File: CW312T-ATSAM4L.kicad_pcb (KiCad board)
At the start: 2 copper layers, 58.7 x 53.7 mm, 30 parts, among them J1 614105150721, P1 PCIEx4 EDGE CONNECTOR, U1 ATSAM4LC2AA-AU

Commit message: updated schematic, pcb, and production files - ready for review
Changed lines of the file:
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@@
 		(tags "resistor")
 		(property "Reference" "R9"
-			(at -0.075 -1.55 360)
+			(at -0.075 -1.55 0)
 			(layer "F.SilkS")
 			(effects
@@
 		)
 		(property "Value" "RES_10k_0603"
-			(at 0 1.43 360)
+			(at 0 1.43 0)
 			(layer "F.Fab")
 			(effects
@@
 		)
 		(fp_text user "${REFERENCE}"
-			(at 0 0 360)
+			(at 0 0 0)
 			(layer "F.Fab")
 			(effects
@@
 		(tags "resistor")
 		(property "Reference" "R2"
-			(at 2.525 0 360)
+			(at 2.525 0 0)
 			(layer "F.SilkS")
 			(effects
@@
 		)
 		(property "Value" "RES_47k_0603"
-			(at 0 1.43 360)
+			(at 0 1.43 0)
 			(layer "F.Fab")
 			(effects
@@
 		)
 		(fp_text user "${REFERENCE}"
-			(at 0 0 360)
+			(at 0 0 0)
 			(layer "F.Fab")
 			(effects
@@
 		(sheetname "Root")
 		(sheetfile "CW312T-ATSAM4L.kicad_sch")
-		(attr smd)
+		(attr smd dnp)
 		(fp_line
 			(start -0.14058 -0.51)
@@
 		(tags "capacitor")
 		(property "Reference" "C2"
-			(at 2.525 0.06 360)
+			(at 2.525 0.06 0)
 			(layer "F.SilkS")
 			(effects
@@
 		)
 		(property "Value" "CAP_2u2_6.3V_0603"
-			(at 0 1.43 360)
+			(at 0 1.43 0)
 			(layer "F.Fab")
 			(effects
@@
 		)
 		(fp_text user "${REFERENCE}"
-			(at 0 0 360)
+			(at 0 0 0)
 			(layer "F.Fab")
 			(effects
@@
 		(sheetname "Root")
 		(sheetfile "CW312T-ATSAM4L.kicad_sch")
-		(attr through_hole)
+		(attr through_hole dnp)
 		(fp_line
 			(start -2.85 -1.38)
@@
 		(tags "capacitor")
 		(property "Reference" "C1"
-			(at -2.525 0 360)
+			(at -2.525 0 0)
 			(layer "F.SilkS")
 			(effects
@@
 		)
 		(property "Value" "CAP_100n_10V_0603"
-			(at 0 1.43 360)
+			(at 0 1.43 0)
 			(layer "F.Fab")
 			(effects
@@
 		)
 		(fp_text user "${REFERENCE}"
-			(at 0 0 360)
+			(at 0 0 0)
 			(layer "F.Fab")
 			(effects
@@
 		(tags "capacitor")
 		(property "Reference" "C12"
-			(at 0 1.95 360)
+			(at 0 1.95 0)
 			(layer "F.SilkS")
 			(effects
@@
 		)
 		(property "Value" "CAP_2u2_6.3V_0603"
-			(at 0 1.43 360)
+			(at 0 1.43 0)
 			(layer "F.Fab")
 			(effects
@@
 		)
 		(fp_text user "${REFERENCE}"
-			(at 0 0 360)
+			(at 0 0 0)
 			(layer "F.Fab")
 			(effects
@@
 		(tags "resistor")
 		(property "Reference" "R7"
-			(at -2.4 -0.1 360)
+			(at -2.4 -0.1 0)
 			(layer "F.SilkS")
 			(effects
@@
 		)
 		(property "Value" "RES_1k5_0603"
-			(at 0 1.43 360)
+			(at 0 1.43 0)
 			(layer "F.Fab")
 			(effects
@@
 		)
 		(fp_text user "${REFERENCE}"
-			(at 0 0 360)
+			(at 0 0 0)
 			(layer "F.Fab")
 			(effects
@@
 		(tags "LQFP QFP")
 		(property "Reference" "U1"
-			(at 4.300001 4.5375 360)
+			(at 4.300001 4.5375 0)
 			(layer "F.SilkS")
 			(effects
@@
 		)
 		(property "Value" "ATSAM4LC2AA-AU"
-			(at 0 5.85 360)
+			(at 0 5.85 0)
 			(layer "F.Fab")
 			(effects
@@
 		)
 		(fp_text user "${REFERENCE}"
-			(at 0 0 360)
+			(at 0 0 0)
 			(layer "F.Fab")
 			(effects
@@
 		(tags "capacitor")
 		(property "Reference" "C10"
-			(at 2.975 -0.05 360)
+			(at 2.975 -0.05 0)
 			(layer "F.SilkS")
 			(effects
@@
 		)
 		(property "Value" "CAP_100n_10V_0603"
-			(at 0 1.43 360)
+			(at 0 1.43 0)
 			(layer "F.Fab")
 			(effects
@@
 		)
 		(fp_text user "${REFERENCE}"
-			(at 0 0 360)
+			(at 0 0 0)
 			(layer "F.Fab")
 			(effects
@@
 		(tags "capacitor")
 		(property "Reference" "C3"
-			(at -2.45 0 360)
+			(at -2.45 0 0)
 			(layer "F.SilkS")
 			(effects
@@
 		)
 		(property "Value" "CAP_47p_50V_0603"
-			(at 0 1.43 360)
+			(at 0 1.43 0)
 			(layer "F.Fab")
 			(effects
@@
 		(sheetname "Root")
 		(sheetfile "CW312T-ATSAM4L.kicad_sch")
-		(attr smd)
+		(attr smd dnp)
 		(fp_line
 			(start -0.140581 0.51)
@@
 		)
 		(fp_text user "${REFERENCE}"
-			(at 0 0 360)
+			(at 0 0 0)
 			(layer "F.Fab")
 			(effects
@@
 	)
 	(gr_text "SAM4L Target Board \nFor ChipWhisperer \nCW312T Board"
-		(at 162.2 78.8 0)
+		(at 162.15 79.1 0)
 		(layer "F.SilkS")
 		(effects
@@
 		(polygon
 			(pts
-				(xy 110.65 55.3) (xy 173.7 55.3) (xy 173.7 114.15) (xy 173.7 114.15) (xy 110.65 114.15)
+				(xy 110.65 55.3) (xy 173.7 55.3) (xy 173.7 114.15) (xy 110.65 114.15)
 			)
 		)

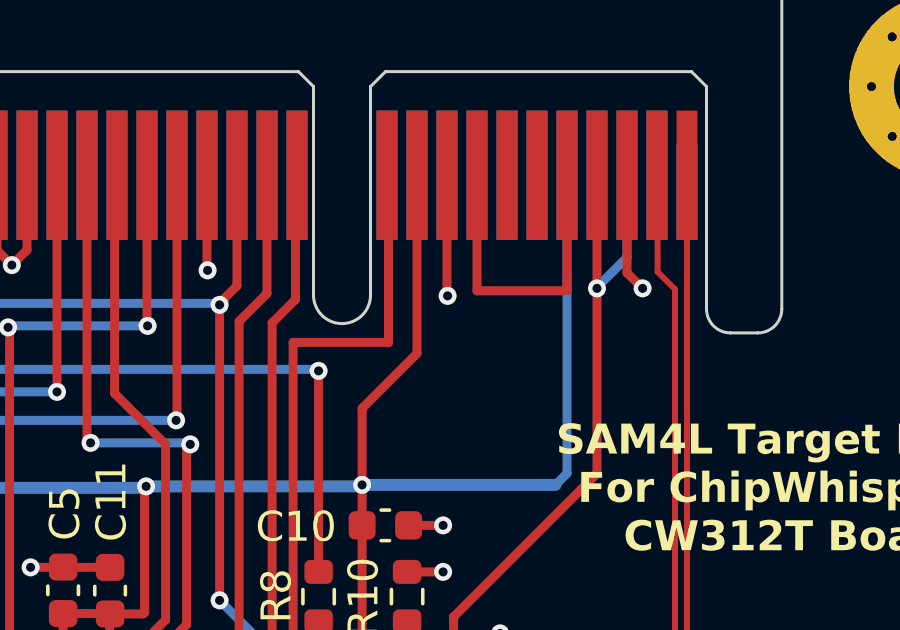
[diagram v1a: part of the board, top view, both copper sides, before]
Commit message: updated silkscreen, schematic notes, and production files
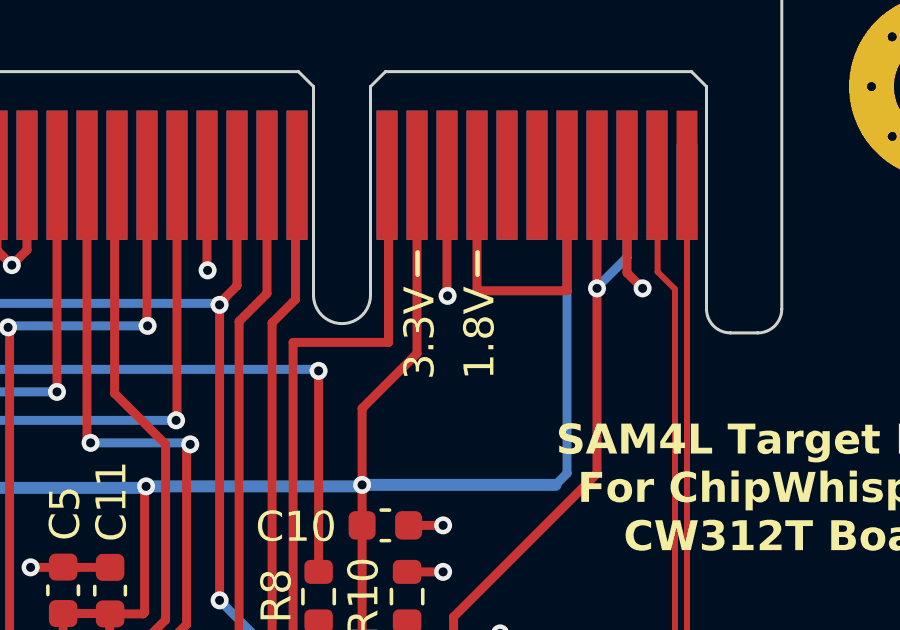
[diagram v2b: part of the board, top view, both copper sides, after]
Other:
- board text added: "1.8V"
- board text added: "3.3V"
- board text added: "RST"
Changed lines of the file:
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@@
 		)
+	)
+	(gr_line
+		(start 126.6 69.05)
+		(end 126.6 69.8)
+		(stroke
+			(width 0.15)
+			(type default)
+		)
+		(layer "B.SilkS")
+	)
+	(gr_line
+		(start 149.6 69.05)
+		(end 149.6 69.8)
+		(stroke
+			(width 0.15)
+			(type default)
+		)
+		(layer "F.SilkS")
+	)
+	(gr_line
+		(start 151.6 69.05)
+		(end 151.6 69.8)
+		(stroke
+			(width 0.15)
+			(type default)
+		)
+		(layer "F.SilkS")
 	)
 	(gr_rect
@@
 		(fill none)
 		(layer "F.SilkS")
+	)
+	(gr_text "RST"
+		(at 125.95 72.6 -90)
+		(layer "B.SilkS")
+		(effects
+			(font
+				(size 1 1)
+				(thickness 0.15)
+			)
+			(justify left bottom mirror)
+		)
 	)
 	(gr_text "NewAE Technology Inc.\nNAE-CW312T-SAM4L\nRoHS / Pb Free"
@@
 		)
 	)
+	(gr_text "3.3V"
+		(at 150.25 73.3 90)
+		(layer "F.SilkS")
+		(effects
+			(font
+				(size 1 1)
+				(thickness 0.15)
+			)
+			(justify left bottom)
+		)
+	)
 	(gr_text "USB"
 		(at 132.45 109 0)
@@
 			)
 			(justify left bottom)
+		)
+	)
+	(gr_text "1.8V"
+		(at 152.25 73.3 90)
+		(layer "F.SilkS")
+		(effects
+			(font
+				(size 1 1)
+				(thickness 0.15)
+			)
+			(justify left bottom)

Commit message: updated schematic and pcb after library re-organization
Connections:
- J1 pad 5: unconnected-(J1-GND-Pad5) -> GND
